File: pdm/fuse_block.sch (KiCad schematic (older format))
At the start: 14 parts, among them Q3 Q_NPN_BCE, Q8 MMBT3904, U12 BTS443P

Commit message: changed to molex headers
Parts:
- added TP5, TP6: TestPoint_Probe, TestPoint:TestPoint_Pad_D1.0mm, symbol Connector:TestPoint_Probe
- C14: renamed from C12; value 7.2uF -> 10uF; footprint Capacitor_SMD:C_0805_2012Metric_Pad1.15x1.40mm_HandSolder -> Capacitor_Tantalum_SMD:CP_EIA-3216-18_Kemet-A_Pad1.58x1.35mm_HandSolder; symbol Device:C -> Device:CP; Digi-Key_PN (none) -> T494A106M020AT
- renumbered D9 to D5, F5 to F2, H5 to H4, Q8 to Q5, Q3 to Q6, R38 to R14, R19 to R15, R20 to R16, R31 to R17, R21 to R18, R22 to R19, R26 to R20, U12 to U5
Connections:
- net sense: now also TP5.1
- net vload: now also TP6.1
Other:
- note removed: "Add lowpass filter"
- note removed: "Change to pull down \nresistor - kinda"

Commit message: changed layout with two plugs
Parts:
- removed H4: MountingHole_Pad, MountingHole:MountingHole_4mm_Pad_Via, symbol Mechanical:MountingHole_Pad
- C14: symbol Device:CP -> pdm-rescue:CP-Device
- D5: symbol Device:LED -> pdm-rescue:LED-Device
- F2: footprint Fuse:blade_fuse_panelized -> pdm_v2:fuseHolder; symbol Device:Fuse -> pdm-rescue:Fuse-Device
- Q5: symbol Transistor_BJT:MMBT3904 -> pdm-rescue:MMBT3904-Transistor_BJT
- Q6: symbol Device:Q_NPN_BCE -> pdm-rescue:Q_NPN_BCE-Device
- R14: symbol Device:R -> pdm-rescue:R-Device
- R15, R16, R17, R18, R19, R20: footprint Resistor_SMD:R_0805_2012Metric_Pad1.15x1.40mm_HandSolder -> Resistor_SMD:R_0805_2012Metric_Pad1.20x1.40mm_HandSolder; symbol Device:R -> pdm-rescue:R-Device
- TP5, TP6: symbol Connector:TestPoint_Probe -> pdm-rescue:TestPoint_Probe-Connector
- U5: symbol Power_Management:BTS443P -> pdm-rescue:BTS443P-Power_Management
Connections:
- net vload renamed Vout
- net vout renamed out
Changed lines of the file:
@@
 $Descr A4 11693 8268
 encoding utf-8
-Sheet 6 6
-Title ""
-Date ""
+Sheet 4 6
+Title "PDM Board"
+Date "2021-01-14"
 Rev ""
-Comp ""
+Comp "UWA Motorsports"
 Comment1 ""
 Comment2 ""
@@
 $EndDescr
 $Comp
-L Power_Management:BTS443P U?
+L pdm-rescue:BTS443P-Power_Management U?
 U 1 1 5F95464C
 P 5750 3600
@@
 $EndComp
 $Comp
-L power:+12V #PWR?
+L pdm-rescue:+12V-power #PWR?
 U 1 1 5F954653
 P 5750 3150
@@
 AR Path="/5F956034/5F954653" Ref="#PWR059"  Part="1"
 AR Path="/5F9560D2/5F954653" Ref="#PWR066"  Part="1"
-F 0 "#PWR066" H 5750 3000 50  0001 C CNN
+F 0 "#PWR038" H 5750 3000 50  0001 C CNN
 F 1 "+12V" H 5765 3323 50  0000 C CNN
 F 2 "" H 5750 3150 50  0001 C CNN
@@
 	5750 3150 5750 3300
 $Comp
-L Device:R R?
+L pdm-rescue:R-Device R?
 U 1 1 5F95465A
 P 5150 4050
@@
 F 0 "R37" V 5050 4050 50  0000 C CNN
 F 1 "220R" V 5150 4050 50  0000 C CNN
-F 2 "Resistor_SMD:R_0805_2012Metric_Pad1.15x1.40mm_HandSolder" V 5080 4050 50  0001 C CNN
+F 2 "Resistor_SMD:R_0805_2012Metric_Pad1.20x1.40mm_HandSolder" V 5080 4050 50  0001 C CNN
 F 3 "~" H 5150 4050 50  0001 C CNN
 	1    5150 4050
@@
 	5300 3500 5450 3500
 $Comp
-L Device:R R?
+L pdm-rescue:R-Device R?
 U 1 1 5F954666
 P 5150 3500
@@
 F 0 "R36" V 5050 3500 50  0000 C CNN
 F 1 "220R" V 5150 3500 50  0000 C CNN
-F 2 "Resistor_SMD:R_0805_2012Metric_Pad1.15x1.40mm_HandSolder" V 5080 3500 50  0001 C CNN
+F 2 "Resistor_SMD:R_0805_2012Metric_Pad1.20x1.40mm_HandSolder" V 5080 3500 50  0001 C CNN
 F 3 "~" H 5150 3500 50  0001 C CNN
 	1    5150 3500
@@
 $EndComp
 $Comp
-L Device:Fuse F?
+L pdm-rescue:Fuse-Device F?
 U 1 1 5F95466C
 P 6450 3600
@@
 F 0 "F5" V 6253 3600 50  0000 C CNN
 F 1 "Fuse" V 6344 3600 50  0000 C CNN
-F 2 "Fuse:blade_fuse_panelized" V 6380 3600 50  0001 C CNN
+F 2 "pdm_v2:fuseHolder" V 6380 3600 50  0001 C CNN
 F 3 "~" H 6450 3600 50  0001 C CNN
 	1    6450 3600
 	0    1    1    0
 $EndComp
-$Comp
-L Mechanical:MountingHole_Pad H?
-U 1 1 5F954678
-P 7800 3600
-AR Path="/5F954678" Ref="H?"  Part="1"
-AR Path="/5F94FFF3/5F954678" Ref="H4"  Part="1"
-AR Path="/5F955EE4/5F954678" Ref="H3"  Part="1"
-AR Path="/5F955F6E/5F954678" Ref="H5"  Part="1"
-AR Path="/5F956034/5F954678" Ref="H6"  Part="1"
-AR Path="/5F9560D2/5F954678" Ref="H7"  Part="1"
-F 0 "H7" V 7754 3750 50  0000 L CNN
-F 1 "MountingHole_Pad" V 7845 3750 50  0000 L CNN
-F 2 "MountingHole:MountingHole_4mm_Pad_Via" H 7800 3600 50  0001 C CNN
-F 3 "~" H 7800 3600 50  0001 C CNN
-	1    7800 3600
-	0    1    1    0
-$EndComp
 Wire Wire Line
 	6600 3600 6750 3600
@@
 	6750 3600 7050 3600
 $Comp
-L Device:R R?
+L pdm-rescue:R-Device R?
 U 1 1 5F954690
 P 6750 3900
@@
 F 0 "R39" V 6650 3900 50  0000 C CNN
 F 1 "2k2" V 6750 3900 50  0000 C CNN
-F 2 "Resistor_SMD:R_0805_2012Metric_Pad1.15x1.40mm_HandSolder" V 6680 3900 50  0001 C CNN
+F 2 "Resistor_SMD:R_0805_2012Metric_Pad1.20x1.40mm_HandSolder" V 6680 3900 50  0001 C CNN
 F 3 "~" H 6750 3900 50  0001 C CNN
 	1    6750 3900
@@
 $EndComp
 $Comp
-L power:GND #PWR?
+L pdm-rescue:GND-power #PWR?
 U 1 1 5F954696
 P 6750 5050
@@
 AR Path="/5F956034/5F954696" Ref="#PWR060"  Part="1"
 AR Path="/5F9560D2/5F954696" Ref="#PWR067"  Part="1"
-F 0 "#PWR067" H 6750 4800 50  0001 C CNN
+F 0 "#PWR039" H 6750 4800 50  0001 C CNN
 F 1 "GND" H 6755 4877 50  0000 C CNN
 F 2 "" H 6750 5050 50  0001 C CNN
@@
 sense
 Text Label 6050 3600 0    50   ~ 0
-vout
+out
 Wire Wire Line
 	6050 3600 6300 3600
@@
 vload
 $Comp
-L Device:Q_NPN_BCE Q6
+L pdm-rescue:Q_NPN_BCE-Device Q6
 U 1 1 5F982D06
 P 7450 4500
@@
 $EndComp
 $Comp
-L Device:R R?
+L pdm-rescue:R-Device R?
 U 1 1 5F954672
 P 6750 4650
@@
 F 0 "R40" H 6800 4650 50  0000 L CNN
 F 1 "220R" V 6750 4550 50  0000 L CNN
-F 2 "Resistor_SMD:R_0805_2012Metric_Pad1.15x1.40mm_HandSolder" V 6680 4650 50  0001 C CNN
+F 2 "Resistor_SMD:R_0805_2012Metric_Pad1.20x1.40mm_HandSolder" V 6680 4650 50  0001 C CNN
 F 3 "~" H 6750 4650 50  0001 C CNN
 	1    6750 4650
@@
 	6750 4300 7450 4300
 $Comp
-L power:+3.3V #PWR?
+L pdm-rescue:+3.3V-power #PWR?
 U 1 1 5F98797F
 P 8550 4400
@@
 AR Path="/5F956034/5F98797F" Ref="#PWR062"  Part="1"
 AR Path="/5F9560D2/5F98797F" Ref="#PWR069"  Part="1"
-F 0 "#PWR069" H 8550 4250 50  0001 C CNN
+F 0 "#PWR041" H 8550 4250 50  0001 C CNN
 F 1 "+3.3V" H 8565 4573 50  0000 C CNN
 F 2 "" H 8550 4400 50  0001 C CNN
@@
 Connection ~ 5150 3700
 $Comp
-L power:GND #PWR?
+L pdm-rescue:GND-power #PWR?
 U 1 1 5FDDFF0E
 P 5150 4300
@@
 AR Path="/5F956034/5FDDFF0E" Ref="#PWR058"  Part="1"
 AR Path="/5F9560D2/5FDDFF0E" Ref="#PWR065"  Part="1"
-F 0 "#PWR065" H 5150 4050 50  0001 C CNN
+F 0 "#PWR037" H 5150 4050 50  0001 C CNN
 F 1 "GND" H 5155 4127 50  0000 C CNN
 F 2 "" H 5150 4300 50  0001 C CNN
@@
 	5150 4300 5150 4200
 $Comp
-L Device:CP C?
+L pdm-rescue:CP-Device C?
 U 1 1 5FDE3A85
 P 4800 4050
@@
 	4800 3700 5150 3700
 $Comp
-L power:GND #PWR?
+L pdm-rescue:GND-power #PWR?
 U 1 1 5FDE452B
 P 4800 4300
@@
 AR Path="/5F956034/5FDE452B" Ref="#PWR057"  Part="1"
 AR Path="/5F9560D2/5FDE452B" Ref="#PWR064"  Part="1"
-F 0 "#PWR064" H 4800 4050 50  0001 C CNN
+F 0 "#PWR036" H 4800 4050 50  0001 C CNN
 F 1 "GND" H 4805 4127 50  0000 C CNN
 F 2 "" H 4800 4300 50  0001 C CNN
@@
 	5900 2600 6000 2600
 $Comp
-L Device:R R?
+L pdm-rescue:R-Device R?
 U 1 1 5F986EB2
 P 5750 2600
@@
 F 0 "R38" V 5650 2600 50  0000 C CNN
 F 1 "220R" V 5750 2600 50  0000 C CNN
-F 2 "Resistor_SMD:R_0805_2012Metric_Pad1.15x1.40mm_HandSolder" V 5680 2600 50  0001 C CNN
+F 2 "Resistor_SMD:R_0805_2012Metric_Pad1.20x1.40mm_HandSolder" V 5680 2600 50  0001 C CNN
 F 3 "~" H 5750 2600 50  0001 C CNN
 	1    5750 2600
@@
 $EndComp
 $Comp
-L Device:LED D5
+L pdm-rescue:LED-Device D5
 U 1 1 5F98650F
 P 6150 2600
@@
 make sure led can handle appropriate back voltage
 $Comp
-L Device:R R?
+L pdm-rescue:R-Device R?
 U 1 1 5FDFC164
 P 8200 4600
@@
 F 0 "R41" V 8100 4600 50  0000 C CNN
 F 1 "2k2" V 8200 4600 50  0000 C CNN
-F 2 "Resistor_SMD:R_0805_2012Metric_Pad1.15x1.40mm_HandSolder" V 8130 4600 50  0001 C CNN
+F 2 "Resistor_SMD:R_0805_2012Metric_Pad1.20x1.40mm_HandSolder" V 8130 4600 50  0001 C CNN
 F 3 "~" H 8200 4600 50  0001 C CNN
 	1    8200 4600
@@
 	7850 4600 8050 4600
 $Comp
-L power:GND #PWR?
+L pdm-rescue:GND-power #PWR?
 U 1 1 5FDFEAE6
 P 7100 5050
@@
 AR Path="/5F956034/5FDFEAE6" Ref="#PWR061"  Part="1"
 AR Path="/5F9560D2/5FDFEAE6" Ref="#PWR068"  Part="1"
-F 0 "#PWR068" H 7100 4800 50  0001 C CNN
+F 0 "#PWR040" H 7100 4800 50  0001 C CNN
 F 1 "GND" H 7105 4877 50  0000 C CNN
 F 2 "" H 7100 5050 50  0001 C CNN
@@
 Connection ~ 4900 3500
 $Comp
-L Device:R R?
+L pdm-rescue:R-Device R?
 U 1 1 5FD390C1
 P 3450 3500
@@
 $EndComp
 $Comp
-L power:+3.3V #PWR?
+L pdm-rescue:+3.3V-power #PWR?
 U 1 1 5FD39CF7
 P 3200 2900
@@
 AR Path="/5F956034/5FD39CF7" Ref="#PWR056"  Part="1"
 AR Path="/5F9560D2/5FD39CF7" Ref="#PWR063"  Part="1"
-F 0 "#PWR063" H 3200 2750 50  0001 C CNN
+F 0 "#PWR035" H 3200 2750 50  0001 C CNN
 F 1 "+3.3V" H 3215 3073 50  0000 C CNN
 F 2 "" H 3200 2900 50  0001 C CNN
@@
 	3200 3500 3300 3500
 $Comp
-L Transistor_BJT:MMBT3904 Q5
+L pdm-rescue:MMBT3904-Transistor_BJT Q5
 U 1 1 5FD300CB
 P 3900 3400
@@
 	7050 3600 7450 3600
 $Comp
-L Connector:TestPoint_Probe TP6
+L pdm-rescue:TestPoint_Probe-Connector TP6
 U 1 1 5FFEFF01
 P 7450 3400
@@
 	7450 3400 7450 3600
 Connection ~ 7450 3600
-Wire Wire Line
-	7450 3600 7700 3600
-$Comp
-L Connector:TestPoint_Probe TP5
+$Comp
+L pdm-rescue:TestPoint_Probe-Connector TP5
 U 1 1 5FFF1F4F
 P 4000 4200
@@
 Wire Wire Line
 	4000 4200 4300 4200
+Wire Wire Line
+	7450 3600 8550 3600
+Text HLabel 8550 3600 2    50   Output ~ 0
+Vout
 $EndSCHEMATC

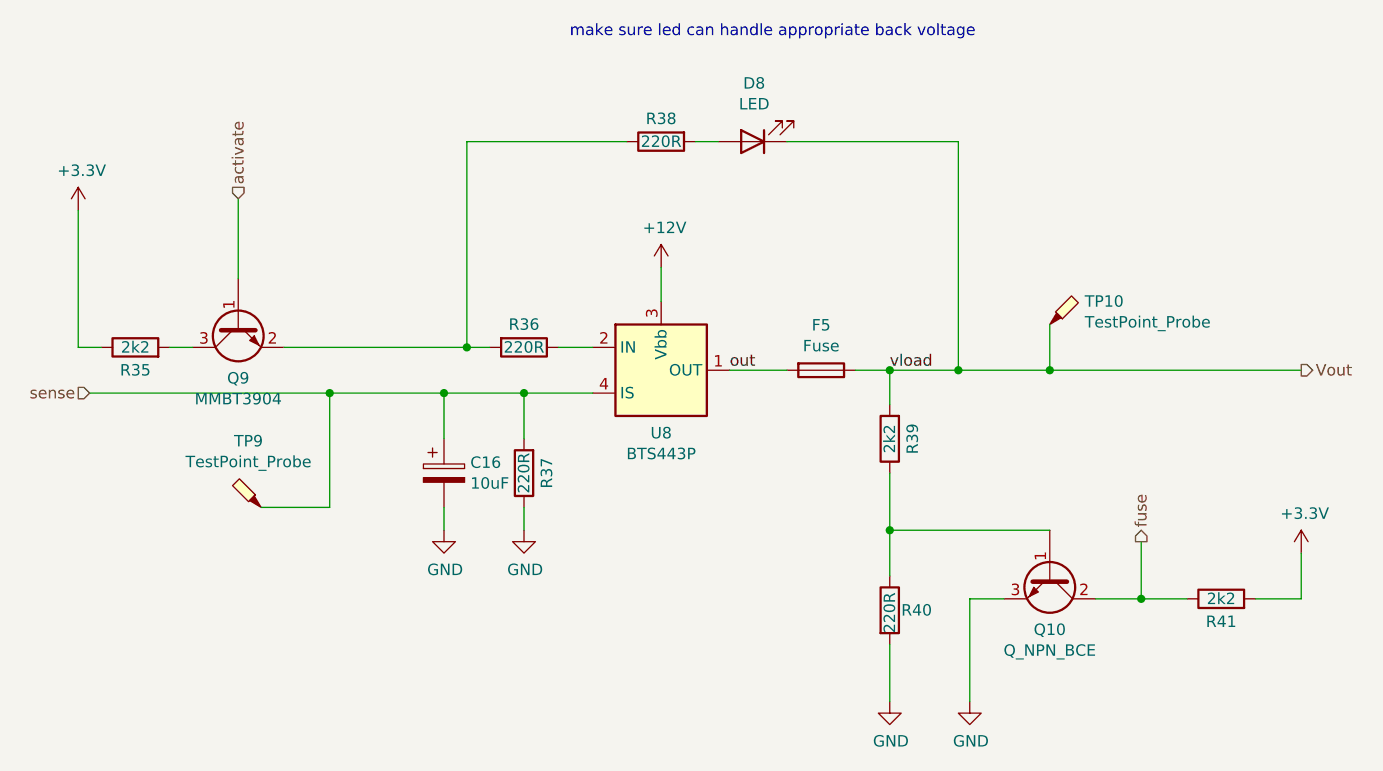
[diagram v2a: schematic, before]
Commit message: added mounting holes again
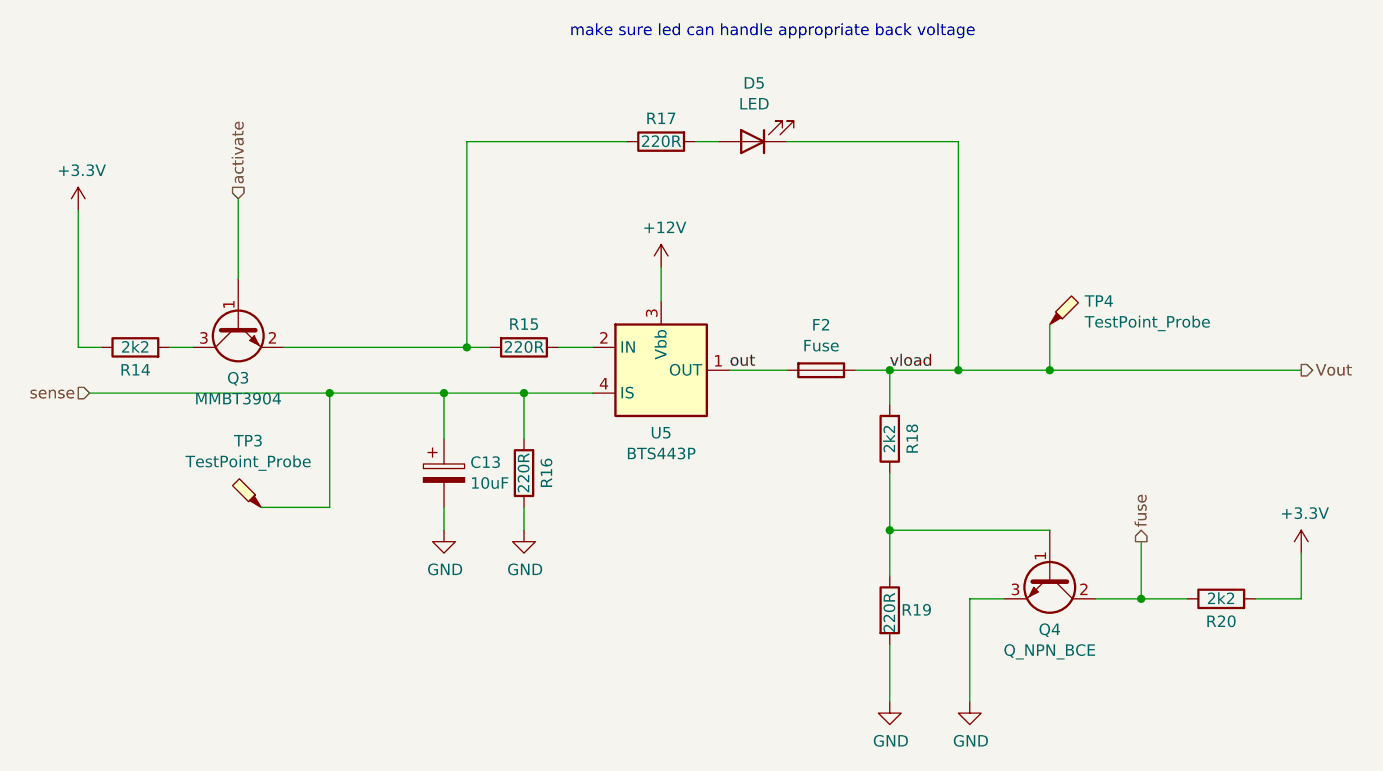
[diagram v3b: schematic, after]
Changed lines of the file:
@@
 $Descr A4 11693 8268
 encoding utf-8
-Sheet 4 6
+Sheet 5 6
 Title "PDM Board"
 Date "2021-01-14"
@@
 AR Path="/5F956034/5F95464C" Ref="U7"  Part="1"
 AR Path="/5F9560D2/5F95464C" Ref="U8"  Part="1"
-F 0 "U8" H 5750 3325 50  0000 C CNN
+F 0 "U5" H 5750 3325 50  0000 C CNN
 F 1 "BTS443P" H 5750 3234 50  0000 C CNN
 F 2 "Package_TO_SOT_SMD:TO-252-4" H 5750 3350 50  0001 C CNN
@@
 AR Path="/5F956034/5F95465A" Ref="R30"  Part="1"
 AR Path="/5F9560D2/5F95465A" Ref="R37"  Part="1"
-F 0 "R37" V 5050 4050 50  0000 C CNN
+F 0 "R16" V 5050 4050 50  0000 C CNN
 F 1 "220R" V 5150 4050 50  0000 C CNN
 F 2 "Resistor_SMD:R_0805_2012Metric_Pad1.20x1.40mm_HandSolder" V 5080 4050 50  0001 C CNN
@@
 AR Path="/5F956034/5F954666" Ref="R29"  Part="1"
 AR Path="/5F9560D2/5F954666" Ref="R36"  Part="1"
-F 0 "R36" V 5050 3500 50  0000 C CNN
+F 0 "R15" V 5050 3500 50  0000 C CNN
 F 1 "220R" V 5150 3500 50  0000 C CNN
 F 2 "Resistor_SMD:R_0805_2012Metric_Pad1.20x1.40mm_HandSolder" V 5080 3500 50  0001 C CNN
@@
 AR Path="/5F956034/5F95466C" Ref="F4"  Part="1"
 AR Path="/5F9560D2/5F95466C" Ref="F5"  Part="1"
-F 0 "F5" V 6253 3600 50  0000 C CNN
+F 0 "F2" V 6253 3600 50  0000 C CNN
 F 1 "Fuse" V 6344 3600 50  0000 C CNN
 F 2 "pdm_v2:fuseHolder" V 6380 3600 50  0001 C CNN
@@
 AR Path="/5F956034/5F954690" Ref="R32"  Part="1"
 AR Path="/5F9560D2/5F954690" Ref="R39"  Part="1"
-F 0 "R39" V 6650 3900 50  0000 C CNN
+F 0 "R18" V 6650 3900 50  0000 C CNN
 F 1 "2k2" V 6750 3900 50  0000 C CNN
 F 2 "Resistor_SMD:R_0805_2012Metric_Pad1.20x1.40mm_HandSolder" V 6680 3900 50  0001 C CNN
@@
 AR Path="/5F94FFF3/5F982D06" Ref="Q4"  Part="1"
 AR Path="/5F955EE4/5F982D06" Ref="Q2"  Part="1"
-F 0 "Q10" V 7685 4500 50  0000 C CNN
+F 0 "Q4" V 7685 4500 50  0000 C CNN
 F 1 "Q_NPN_BCE" V 7776 4500 50  0000 C CNN
 F 2 "Package_TO_SOT_SMD:SOT-23_Handsoldering" H 7650 4600 50  0001 C CNN
@@
 AR Path="/5F956034/5F954672" Ref="R33"  Part="1"
 AR Path="/5F9560D2/5F954672" Ref="R40"  Part="1"
-F 0 "R40" H 6800 4650 50  0000 L CNN
+F 0 "R19" H 6800 4650 50  0000 L CNN
 F 1 "220R" V 6750 4550 50  0000 L CNN
 F 2 "Resistor_SMD:R_0805_2012Metric_Pad1.20x1.40mm_HandSolder" V 6680 4650 50  0001 C CNN
@@
 AR Path="/5F955EE4/5FDE3A85" Ref="C12"  Part="1"
 AR Path="/5F956034/5FDE3A85" Ref="C15"  Part="1"
-F 0 "C16" H 4915 4096 50  0000 L CNN
+F 0 "C13" H 4915 4096 50  0000 L CNN
 F 1 "10uF" H 4915 4005 50  0000 L CNN
 F 2 "Capacitor_Tantalum_SMD:CP_EIA-3216-18_Kemet-A_Pad1.58x1.35mm_HandSolder" H 4838 3900 50  0001 C CNN
@@
 AR Path="/5F956034/5F986EB2" Ref="R31"  Part="1"
 AR Path="/5F9560D2/5F986EB2" Ref="R38"  Part="1"
-F 0 "R38" V 5650 2600 50  0000 C CNN
+F 0 "R17" V 5650 2600 50  0000 C CNN
 F 1 "220R" V 5750 2600 50  0000 C CNN
 F 2 "Resistor_SMD:R_0805_2012Metric_Pad1.20x1.40mm_HandSolder" V 5680 2600 50  0001 C CNN
@@
 AR Path="/5F955F6E/5F98650F" Ref="D6"  Part="1"
 AR Path="/5F955EE4/5F98650F" Ref="D4"  Part="1"
-F 0 "D8" H 6143 2345 50  0000 C CNN
+F 0 "D5" H 6143 2345 50  0000 C CNN
 F 1 "LED" H 6143 2436 50  0000 C CNN
 F 2 "LED_SMD:LED_0805_2012Metric_Pad1.15x1.40mm_HandSolder" H 6150 2600 50  0001 C CNN
@@
 AR Path="/5F956034/5FDFC164" Ref="R34"  Part="1"
 AR Path="/5F9560D2/5FDFC164" Ref="R41"  Part="1"
-F 0 "R41" V 8100 4600 50  0000 C CNN
+F 0 "R20" V 8100 4600 50  0000 C CNN
 F 1 "2k2" V 8200 4600 50  0000 C CNN
 F 2 "Resistor_SMD:R_0805_2012Metric_Pad1.20x1.40mm_HandSolder" V 8130 4600 50  0001 C CNN
@@
 AR Path="/5F956034/5FD390C1" Ref="R28"  Part="1"
 AR Path="/5F9560D2/5FD390C1" Ref="R35"  Part="1"
-F 0 "R35" V 3350 3500 50  0000 C CNN
+F 0 "R14" V 3350 3500 50  0000 C CNN
 F 1 "2k2" V 3450 3500 50  0000 C CNN
 F 2 "Resistor_SMD:R_0805_2012Metric_Pad1.20x1.40mm_HandSolder" V 3380 3500 50  0001 C CNN
@@
 AR Path="/5F956034/5FD300CB" Ref="Q7"  Part="1"
 AR Path="/5F9560D2/5FD300CB" Ref="Q9"  Part="1"
-F 0 "Q9" V 4135 3400 50  0000 C CNN
+F 0 "Q3" V 4135 3400 50  0000 C CNN
 F 1 "MMBT3904" V 4226 3400 50  0000 C CNN
 F 2 "Package_TO_SOT_SMD:SOT-23" H 4100 3325 50  0001 L CIN
@@
 AR Path="/5F956034/5FFEFF01" Ref="TP8"  Part="1"
 AR Path="/5F9560D2/5FFEFF01" Ref="TP10"  Part="1"
-F 0 "TP10" H 7603 3501 50  0000 L CNN
+F 0 "TP4" H 7603 3501 50  0000 L CNN
 F 1 "TestPoint_Probe" H 7603 3410 50  0000 L CNN
 F 2 "TestPoint:TestPoint_Pad_D1.0mm" H 7650 3400 50  0001 C CNN
@@
 AR Path="/5F956034/5FFF1F4F" Ref="TP7"  Part="1"
 AR Path="/5F9560D2/5FFF1F4F" Ref="TP9"  Part="1"
-F 0 "TP9" V 4290 4255 50  0000 C CNN
+F 0 "TP3" V 4290 4255 50  0000 C CNN
 F 1 "TestPoint_Probe" V 4199 4255 50  0000 C CNN
 F 2 "TestPoint:TestPoint_Pad_D1.0mm" H 4200 4200 50  0001 C CNN
